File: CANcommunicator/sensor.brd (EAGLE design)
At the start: 33 x 26.2 mm, 28 parts, among them IC1 0.1uF, IC2 1.0uF, IC3 0.1uF

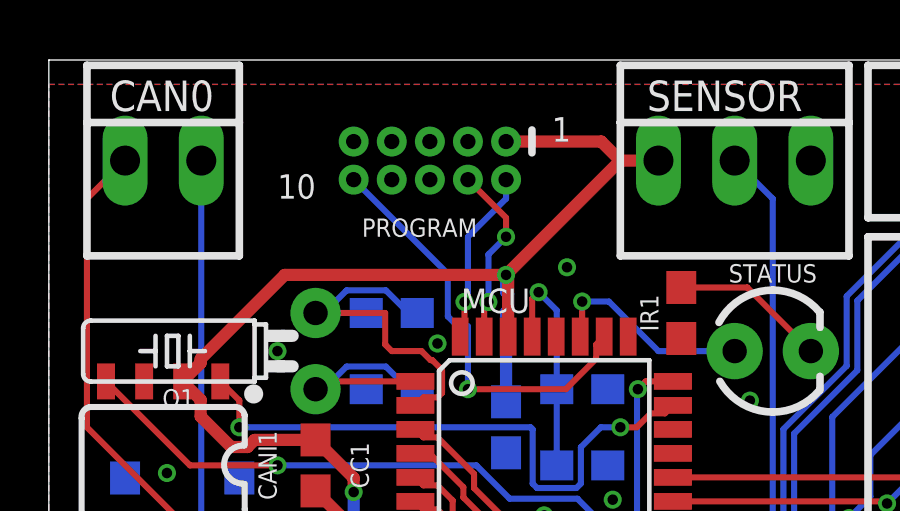
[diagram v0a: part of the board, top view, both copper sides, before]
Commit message: Add pullup on SWDCLK and RC filter on RESET_L
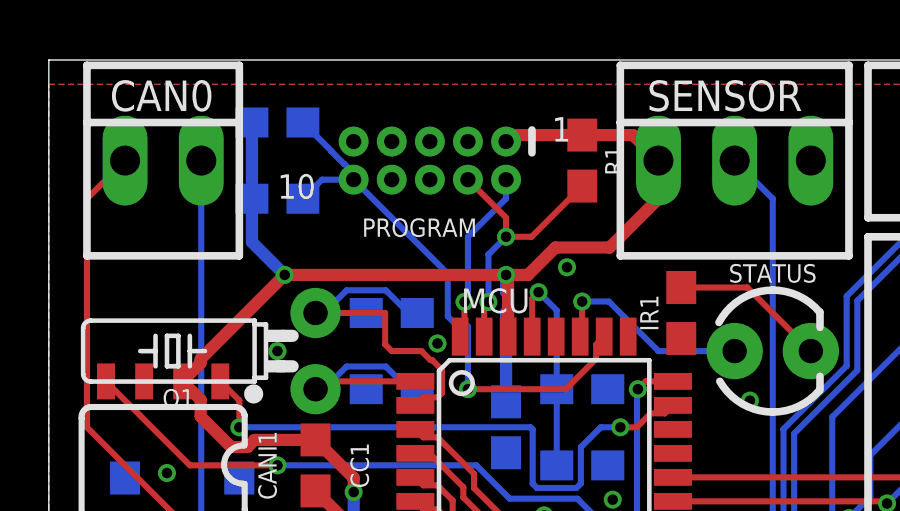
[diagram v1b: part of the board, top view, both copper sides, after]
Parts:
- added C1: 100pF, SparkFun-Capacitors:0603
- added R1: 1k, SparkFun-Resistors:0603
- added R2: 2.2k, SparkFun-Resistors:0603
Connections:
- removed net RESET: MCU.26, PROGRAM.10
- new net RESET_L: C1.2, MCU.26, PROGRAM.10, R2.1
- net SWDCLK: now also R1.2
- net VCC: now also C1.1, R1.1, R2.2
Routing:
- net RESET_L: track 0.00 -> 18.9 mm, vias 0 -> 1
- net RESET: track 14.3 -> 0.00 mm, vias 1 -> 0
- net VCC: track 65.7 -> 73.4 mm, vias 2 -> 3
- net SWDCLK: track 6.06 -> 9.30 mm
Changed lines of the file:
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@@
 <attribute name="OC_NEWARK" value="25C3832" x="30.48" y="23.495" size="1.778" layer="27" rot="R270" display="off"/>
+</element>
+<element name="R1" library="SparkFun-Resistors" library_urn="urn:adsk.eagle:library:532" package="0603" package3d_urn="urn:adsk.eagle:package:39650/1" value="1k" x="17.78" y="22.86" rot="R270">
+<attribute name="NAME" x="18.542" y="22.86" size="0.6096" layer="25" font="vector" ratio="20" rot="R270" align="bottom-center"/>
+<attribute name="PROD_ID" value="RES-07856" x="17.78" y="22.86" size="1.778" layer="27" rot="R270" display="off"/>
+<attribute name="VALUE" x="17.018" y="22.86" size="0.6096" layer="27" font="vector" ratio="20" rot="R270" align="top-center"/>
+</element>
+<element name="R2" library="SparkFun-Resistors" library_urn="urn:adsk.eagle:library:532" package="0603" package3d_urn="urn:adsk.eagle:package:39650/1" value="2.2k" x="7.62" y="24.13" rot="MR0">
+<attribute name="NAME" x="7.62" y="24.892" size="0.6096" layer="26" font="vector" ratio="20" rot="MR0" align="bottom-center"/>
+<attribute name="PROD_ID" value="RES-08272" x="7.62" y="24.13" size="1.778" layer="28" rot="MR0" display="off"/>
+<attribute name="VALUE" x="7.62" y="23.368" size="0.6096" layer="28" font="vector" ratio="20" rot="MR0" align="top-center"/>
+</element>
+<element name="C1" library="SparkFun-Capacitors" library_urn="urn:adsk.eagle:library:510" package="0603" package3d_urn="urn:adsk.eagle:package:37414/1" value="100pF" x="7.62" y="21.59" rot="MR180">
+<attribute name="NAME" x="7.62" y="20.828" size="0.6096" layer="26" font="vector" ratio="20" rot="MR180" align="bottom-center"/>
+<attribute name="PROD_ID" value="CAP-07883" x="7.62" y="21.59" size="1.778" layer="28" rot="MR180" display="off"/>
+<attribute name="VALUE" x="7.62" y="22.352" size="0.6096" layer="28" font="vector" ratio="20" rot="MR180" align="top-center"/>
 </element>
 </elements>
@@
 <wire x1="15.31" y1="18.98" x2="15.31" y2="16.9926" width="0.4064" layer="1"/>
 <wire x1="7.86210625" y1="19.05" x2="15.24" y2="19.05" width="0.4064" layer="1"/>
-<wire x1="15.24" y1="19.05" x2="19.05" y2="22.86" width="0.4064" layer="1"/>
-<wire x1="19.05" y1="22.86" x2="20.32" y2="22.86" width="0.4064" layer="1"/>
-<wire x1="15.24" y1="23.495" x2="18.415" y2="23.495" width="0.4064" layer="1"/>
-<wire x1="18.415" y1="23.495" x2="19.05" y2="22.86" width="0.4064" layer="1"/>
 <via x="15.24" y="19.05" extent="1-16" drill="0.35"/>
 <wire x1="15.24" y1="19.05" x2="15.24" y2="18.48840625" width="0.4064" layer="16"/>
@@
 <wire x1="14.6557875" y1="4.7004" x2="23.4442125" y2="4.7004" width="1.016" layer="16"/>
 <wire x1="11.43" y1="6.77" x2="11.43" y2="2.54" width="1.016" layer="16"/>
+<contactref element="R1" pad="1"/>
+<contactref element="R2" pad="2"/>
+<contactref element="C1" pad="1"/>
+<wire x1="15.24" y1="19.05" x2="15.9723875" y2="19.05" width="0.4064" layer="1"/>
+<wire x1="15.9723875" y1="19.05" x2="16.8839875" y2="19.9616" width="0.4064" layer="1"/>
+<wire x1="16.8839875" y1="19.9616" x2="18.6916" y2="19.9616" width="0.4064" layer="1"/>
+<wire x1="20.32" y1="21.59" x2="20.32" y2="22.86" width="0.4064" layer="1"/>
+<wire x1="18.6916" y1="19.9616" x2="20.32" y2="21.59" width="0.4064" layer="1"/>
+<wire x1="20.32" y1="22.86" x2="19.47" y2="23.71" width="0.4064" layer="1"/>
+<wire x1="19.47" y1="23.71" x2="17.78" y2="23.71" width="0.4064" layer="1"/>
+<wire x1="17.78" y1="23.71" x2="15.455" y2="23.71" width="0.4064" layer="1"/>
+<wire x1="15.455" y1="23.71" x2="15.24" y2="23.495" width="0.4064" layer="1"/>
+<wire x1="6.77" y1="24.13" x2="6.77" y2="21.59" width="0.4064" layer="16"/>
+<via x="7.86210625" y="19.05" extent="1-16" drill="0.35"/>
+<wire x1="7.86210625" y1="19.05" x2="6.77" y2="20.14210625" width="0.4064" layer="16"/>
+<wire x1="6.77" y1="20.14210625" x2="6.77" y2="21.59" width="0.4064" layer="16"/>
 </signal>
 <signal name="VDDANA">
@@
 <wire x1="15.24" y1="20.32" x2="15.24" y2="20.955" width="0.2032" layer="1"/>
 <wire x1="15.24" y1="20.955" x2="13.97" y2="22.225" width="0.2032" layer="1"/>
-</signal>
-<signal name="RESET">
+<contactref element="R1" pad="2"/>
+<wire x1="15.24" y1="20.32" x2="16.09" y2="20.32" width="0.2032" layer="1"/>
+<wire x1="16.09" y1="20.32" x2="17.78" y2="22.01" width="0.2032" layer="1"/>
+</signal>
+<signal name="RESET_L">
 <contactref element="MCU" pad="26"/>
 <contactref element="PROGRAM" pad="10"/>
@@
 <wire x1="13.97" y1="15.24" x2="17.2310125" y2="15.24" width="0.2032" layer="1"/>
 <wire x1="17.2310125" y1="15.24" x2="18.2434" y2="16.2523875" width="0.2032" layer="1"/>
+<contactref element="R2" pad="1"/>
+<contactref element="C1" pad="2"/>
+<wire x1="10.16" y1="22.44" x2="10.16" y2="22.225" width="0.2032" layer="16"/>
+<wire x1="8.47" y1="24.13" x2="9.406" y2="23.194" width="0.2032" layer="16"/>
+<wire x1="9.406" y1="23.194" x2="9.406" y2="23.18268125" width="0.2032" layer="16"/>
+<wire x1="9.406" y1="23.18268125" x2="9.84768125" y2="22.741" width="0.2032" layer="16"/>
+<wire x1="9.84768125" y1="22.741" x2="9.859" y2="22.741" width="0.2032" layer="16"/>
+<wire x1="9.859" y1="22.741" x2="10.16" y2="22.44" width="0.2032" layer="16"/>
+<wire x1="8.47" y1="21.59" x2="9.105" y2="22.225" width="0.2032" layer="16"/>
+<wire x1="9.105" y1="22.225" x2="10.16" y2="22.225" width="0.2032" layer="16"/>
 </signal>
 <signal name="LEDA">

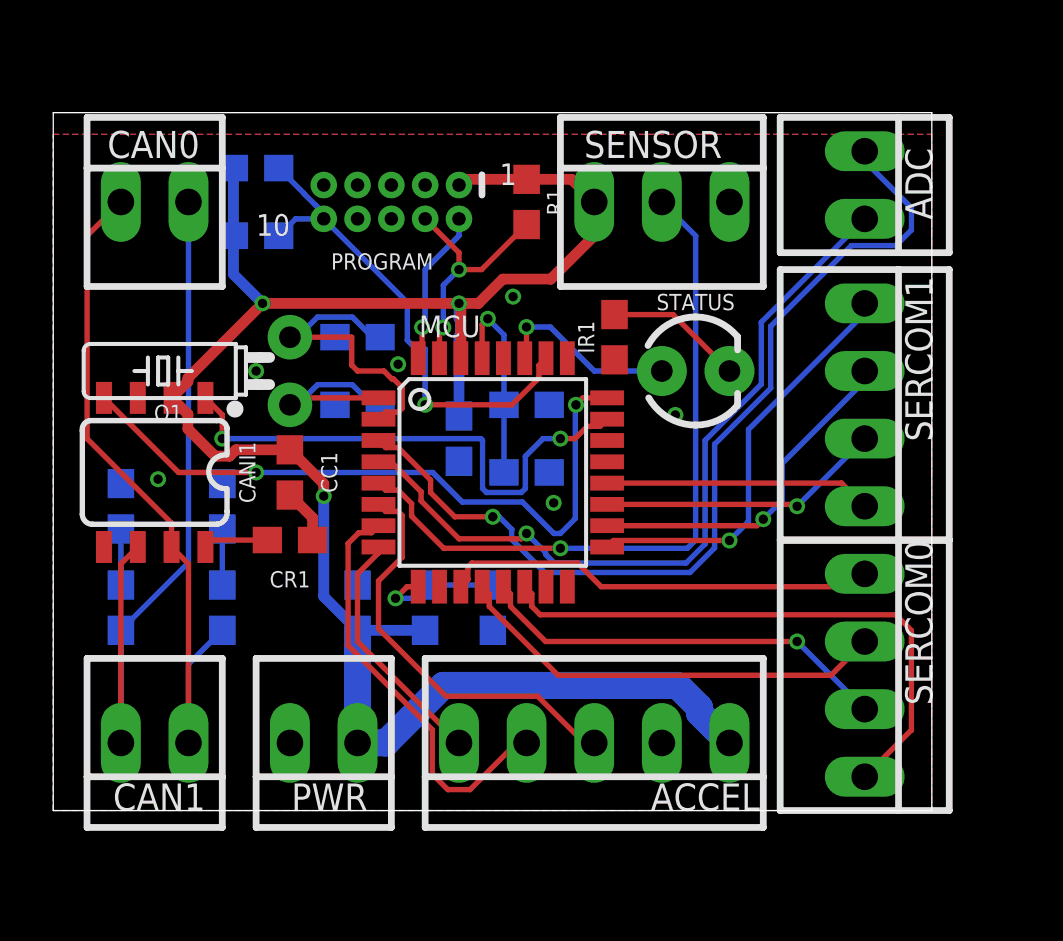
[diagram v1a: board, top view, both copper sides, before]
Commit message: Fix resistor placement by connector, mask vias
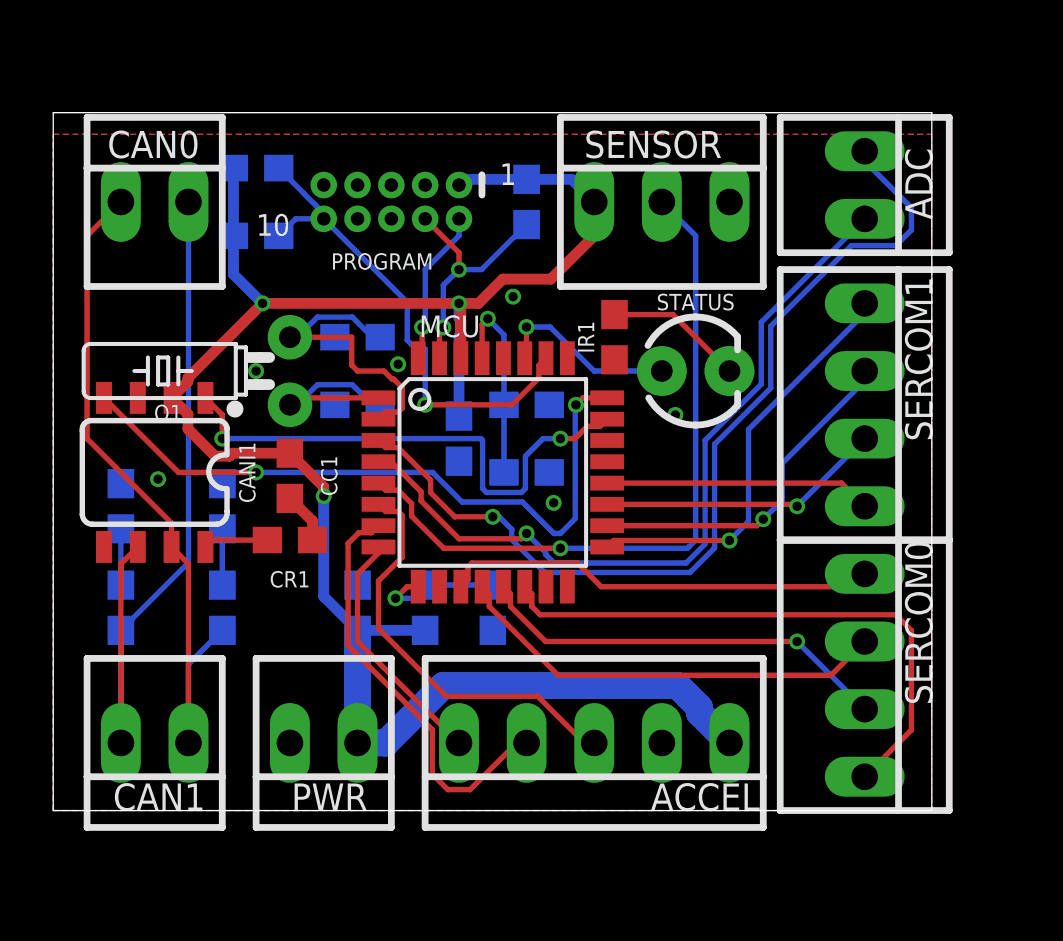
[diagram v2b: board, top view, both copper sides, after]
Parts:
- moved CC1 0.13 mm to (8.89, 12.6)
- flipped R1 to the bottom
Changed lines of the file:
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@@
 <text x="16.764" y="23.495" size="0.8128" layer="21">1</text>
 <text x="7.62" y="21.59" size="0.8128" layer="21">10</text>
-<dimension x1="0" y1="0" x2="0" y2="26.213" x3="-2.54" y3="13.1065" textsize="0.8128" layer="1" unit="inch"/>
-<dimension x1="0" y1="0" x2="33.02" y2="0" x3="16.51" y3="-2.54" textsize="0.8128" layer="1" unit="inch"/>
 </plain>
 <attributes>
@@
 </class>
 </classes>
-<designrules name="oshpark-2layer">
+<designrules name="oshpark-2layer *">
 <description language="en">&lt;b&gt;OSH Park Design Rules&lt;/b&gt;
 &lt;p&gt;
@@
 <param name="mlMinCreamFrame" value="0mil"/>
 <param name="mlMaxCreamFrame" value="0mil"/>
-<param name="mlViaStopLimit" value="0mil"/>
+<param name="mlViaStopLimit" value="20mil"/>
 <param name="srRoundness" value="0"/>
 <param name="srMinRoundness" value="0mil"/>
@@
 <attribute name="VALUE" x="1.778" y="11.43" size="0.6096" layer="28" font="vector" ratio="20" rot="MR90" align="top-center"/>
 </element>
-<element name="CC1" library="SparkFun-Capacitors" library_urn="urn:adsk.eagle:library:510" package="0603" package3d_urn="urn:adsk.eagle:package:37414/1" value="0.1uF" x="8.89" y="12.7" rot="R90">
-<attribute name="NAME" x="10.668" y="12.7" size="0.6096" layer="25" font="vector" ratio="20" rot="R90" align="bottom-center"/>
-<attribute name="PROD_ID" value="CAP-00810" x="44.45" y="31.75" size="1.778" layer="27" rot="R90" display="off"/>
-<attribute name="VALUE" x="9.652" y="12.7" size="0.6096" layer="27" font="vector" ratio="20" rot="R90" align="top-center"/>
+<element name="CC1" library="SparkFun-Capacitors" library_urn="urn:adsk.eagle:library:510" package="0603" package3d_urn="urn:adsk.eagle:package:37414/1" value="0.1uF" x="8.89" y="12.573" rot="R90">
+<attribute name="NAME" x="10.668" y="12.573" size="0.6096" layer="25" font="vector" ratio="20" rot="R90" align="bottom-center"/>
+<attribute name="PROD_ID" value="CAP-00810" x="44.45" y="31.623" size="1.778" layer="27" rot="R90" display="off"/>
+<attribute name="VALUE" x="9.652" y="12.573" size="0.6096" layer="27" font="vector" ratio="20" rot="R90" align="top-center"/>
 </element>
 <element name="PC1" library="SparkFun-Capacitors" library_urn="urn:adsk.eagle:library:510" package="0603" package3d_urn="urn:adsk.eagle:package:37414/1" value="10uF" x="11.43" y="7.62" rot="MR90">
@@
 <attribute name="OC_NEWARK" value="25C3832" x="30.48" y="23.495" size="1.778" layer="27" rot="R270" display="off"/>
 </element>
-<element name="R1" library="SparkFun-Resistors" library_urn="urn:adsk.eagle:library:532" package="0603" package3d_urn="urn:adsk.eagle:package:39650/1" value="1k" x="17.78" y="22.86" rot="R270">
-<attribute name="NAME" x="18.542" y="22.86" size="0.6096" layer="25" font="vector" ratio="20" rot="R270" align="bottom-center"/>
-<attribute name="PROD_ID" value="RES-07856" x="17.78" y="22.86" size="1.778" layer="27" rot="R270" display="off"/>
-<attribute name="VALUE" x="17.018" y="22.86" size="0.6096" layer="27" font="vector" ratio="20" rot="R270" align="top-center"/>
+<element name="R1" library="SparkFun-Resistors" library_urn="urn:adsk.eagle:library:532" package="0603" package3d_urn="urn:adsk.eagle:package:39650/1" value="1k" x="17.78" y="22.86" rot="MR270">
+<attribute name="NAME" x="17.018" y="22.86" size="0.6096" layer="26" font="vector" ratio="20" rot="MR270" align="bottom-center"/>
+<attribute name="PROD_ID" value="RES-07856" x="17.78" y="22.86" size="1.778" layer="28" rot="MR270" display="off"/>
+<attribute name="VALUE" x="18.542" y="22.86" size="0.6096" layer="28" font="vector" ratio="20" rot="MR270" align="top-center"/>
 </element>
 <element name="R2" library="SparkFun-Resistors" library_urn="urn:adsk.eagle:library:532" package="0603" package3d_urn="urn:adsk.eagle:package:39650/1" value="2.2k" x="7.62" y="24.13" rot="MR0">
@@
 </polygon>
 <via x="17.272" y="19.304" extent="1-16" drill="0.35"/>
-<wire x1="8.89" y1="11.85" x2="9.74" y2="11" width="0.4064" layer="1"/>
-<wire x1="9.74" y1="11" x2="9.74" y2="10.16" width="0.4064" layer="1"/>
+<wire x1="9.74" y1="10.873" x2="8.89" y2="11.723" width="0.4064" layer="1"/>
+<wire x1="9.74" y1="10.873" x2="9.74" y2="10.16" width="0.4064" layer="1"/>
 <via x="18.796" y="11.557" extent="1-16" drill="0.35"/>
 <via x="23.368" y="14.859" extent="1-16" drill="0.35"/>
@@
 <wire x1="4.445" y1="15.5" x2="5.0594" y2="14.8856" width="0.4064" layer="1"/>
 <wire x1="6.0776125" y1="13.3124" x2="6.6223875" y2="13.3124" width="0.4064" layer="1"/>
-<wire x1="6.6223875" y1="13.3124" x2="6.8599875" y2="13.55" width="0.4064" layer="1"/>
-<wire x1="6.8599875" y1="13.55" x2="8.89" y2="13.55" width="0.4064" layer="1"/>
+<wire x1="6.6223875" y1="13.3124" x2="6.7329875" y2="13.423" width="0.4064" layer="1"/>
+<wire x1="8.89" y1="13.423" x2="6.7329875" y2="13.423" width="0.4064" layer="1"/>
 <wire x1="5.0594" y1="14.8856" x2="5.0594" y2="14.3306125" width="0.4064" layer="1"/>
 <wire x1="5.0594" y1="14.3306125" x2="6.0776125" y2="13.3124" width="0.4064" layer="1"/>
-<wire x1="8.89" y1="13.55" x2="10.16" y2="12.28" width="0.4064" layer="1"/>
-<wire x1="10.16" y1="12.28" x2="10.16" y2="11.811" width="0.4064" layer="1"/>
+<wire x1="10.16" y1="12.153" x2="8.89" y2="13.423" width="0.4064" layer="1"/>
+<wire x1="10.16" y1="12.153" x2="10.16" y2="11.811" width="0.4064" layer="1"/>
 <via x="10.16" y="11.811" extent="1-16" drill="0.35"/>
 <wire x1="10.16" y1="11.811" x2="10.16" y2="8.04" width="0.4064" layer="16"/>
@@
 <wire x1="20.32" y1="21.59" x2="20.32" y2="22.86" width="0.4064" layer="1"/>
 <wire x1="18.6916" y1="19.9616" x2="20.32" y2="21.59" width="0.4064" layer="1"/>
-<wire x1="20.32" y1="22.86" x2="19.47" y2="23.71" width="0.4064" layer="1"/>
-<wire x1="19.47" y1="23.71" x2="17.78" y2="23.71" width="0.4064" layer="1"/>
-<wire x1="17.78" y1="23.71" x2="15.455" y2="23.71" width="0.4064" layer="1"/>
-<wire x1="15.455" y1="23.71" x2="15.24" y2="23.495" width="0.4064" layer="1"/>
 <wire x1="6.77" y1="24.13" x2="6.77" y2="21.59" width="0.4064" layer="16"/>
 <via x="7.86210625" y="19.05" extent="1-16" drill="0.35"/>
 <wire x1="7.86210625" y1="19.05" x2="6.77" y2="20.14210625" width="0.4064" layer="16"/>
 <wire x1="6.77" y1="20.14210625" x2="6.77" y2="21.59" width="0.4064" layer="16"/>
+<wire x1="15.24" y1="23.495" x2="15.455" y2="23.71" width="0.4064" layer="16"/>
+<wire x1="15.455" y1="23.71" x2="17.78" y2="23.71" width="0.4064" layer="16"/>
+<wire x1="17.78" y1="23.71" x2="19.47" y2="23.71" width="0.4064" layer="16"/>
+<wire x1="19.47" y1="23.71" x2="20.32" y2="22.86" width="0.4064" layer="16"/>
 </signal>
 <signal name="VDDANA">
@@
 <wire x1="15.24" y1="20.955" x2="13.97" y2="22.225" width="0.2032" layer="1"/>
 <contactref element="R1" pad="2"/>
-<wire x1="15.24" y1="20.32" x2="16.09" y2="20.32" width="0.2032" layer="1"/>
-<wire x1="16.09" y1="20.32" x2="17.78" y2="22.01" width="0.2032" layer="1"/>
+<wire x1="17.78" y1="22.01" x2="16.09" y2="20.32" width="0.2032" layer="16"/>
+<wire x1="16.09" y1="20.32" x2="15.24" y2="20.32" width="0.2032" layer="16"/>
 </signal>
 <signal name="RESET_L">

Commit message: Move some signal traces away from capacitors
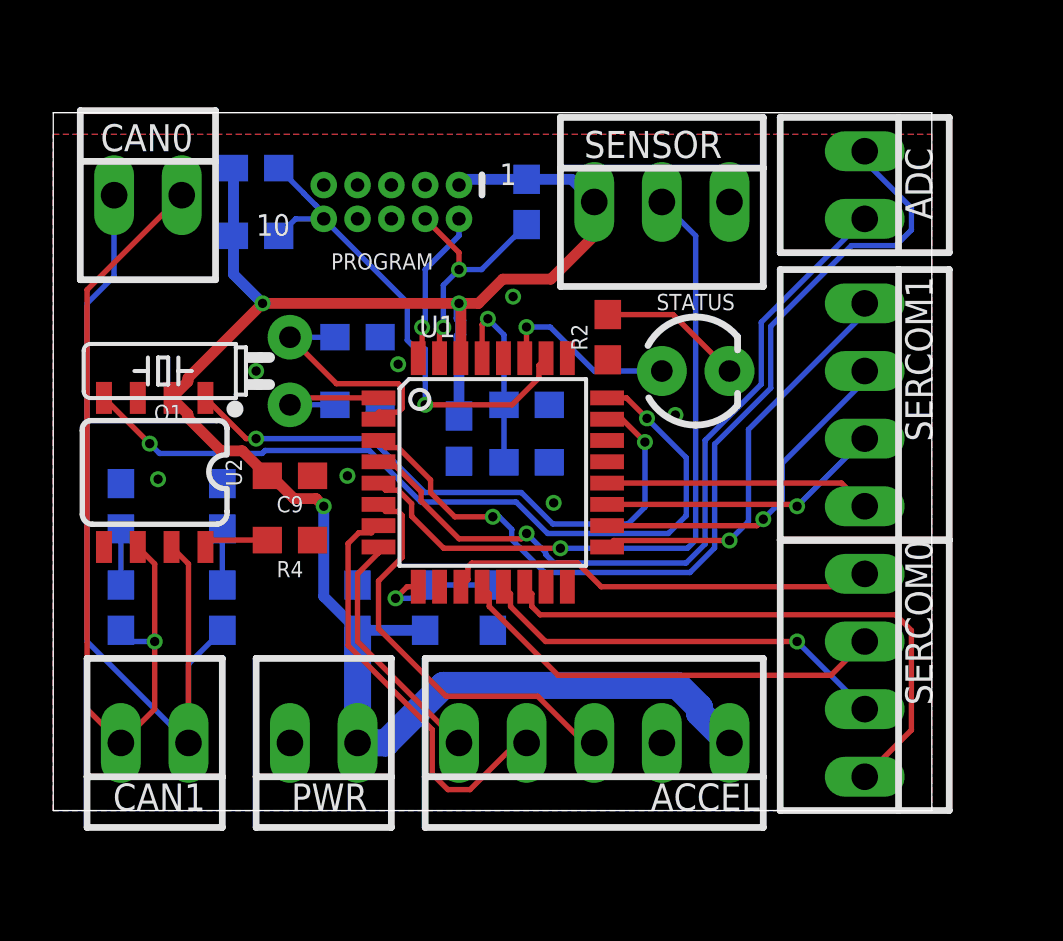
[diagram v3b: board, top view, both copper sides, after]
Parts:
- removed IC3: 0.1uF, SparkFun-Capacitors:0603
- removed IR1: 330, SparkFun-Resistors:0603
- removed PC1: 10uF, SparkFun-Capacitors:0603
- added C5: 0.1uF, SparkFun-Capacitors:0603
- added C6: 100pF, SparkFun-Capacitors:0603
- added R3: 1k, SparkFun-Resistors:0603
- C1: value 100pF -> 10uF
- R1: value 1k -> 2.2k
- R2: value 2.2k -> 330
- moved R2 14.7 mm to (20.8, 17.8), flipped to the top, turned to 90 degrees
- moved C1 14.5 mm to (11.4, 7.62), turned to 90 degrees
- moved R1 10.2 mm to (7.62, 24.1), turned to 0 degrees
- moved CAN0 0.36 mm to (3.56, 23.1)
- turned C7 to 180 degrees
- turned C8 to 180 degrees
- turned C9 to 180 degrees
- renumbered CANI1 to U2, CC1 to C9, CC2 to C10, CC3 to C11, CR1 to R4, CR2 to R5, CR3 to R6, IC1 to C3, IC2 to C4, MCU to U1, OC1 to C7, OC2 to C8, PC2 to C2
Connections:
- net GND: now also C1.2, C5.2, R2.1; no longer IC3.2, IR1.1, PC1.2
- net LEDC: now also R2.2; no longer IR1.2
- net RESET_L: now also C6.2, R1.1; no longer C1.2, R2.1
- net SWDCLK: now also R3.2; no longer R1.2
- net VCC: now also C6.1, R1.2, R3.1; no longer PC1.1, R1.1, R2.2
- net VDDCORE: now also C5.1; no longer IC3.1
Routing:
- net CAN1H: track 27.2 -> 35.0 mm
- net CAN1RX: track 25.6 -> 30.4 mm
- net CAN1L: track 29.0 -> 32.2 mm, vias 0 -> 1
- net CAN1TX: track 20.0 -> 23.0 mm
- net XOUT32: track 11.5 -> 9.02 mm
- net XIN32: track 7.45 -> 5.13 mm
- net GND: track 1.92 -> 0.00 mm, vias 6 -> 7
- net VCC: track 73.3 -> 72.5 mm
